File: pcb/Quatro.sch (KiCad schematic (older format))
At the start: 96 parts, among them J1 BATTERY, J2 BATTERY, J3 Conn_01x02, J4 UART1 SH, J5 st-link SH, J6 2.54mm 02x03, J7 2.54mm 02x03, Q1 IRLML6402, Q2 IRFML8244, Q3 BSS138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

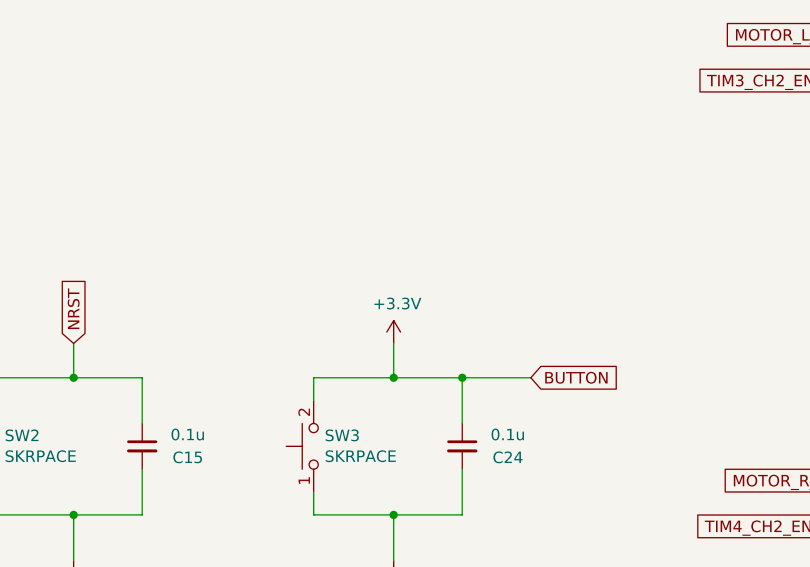
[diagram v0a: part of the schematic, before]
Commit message: プッシュスイッチに抵抗を追加
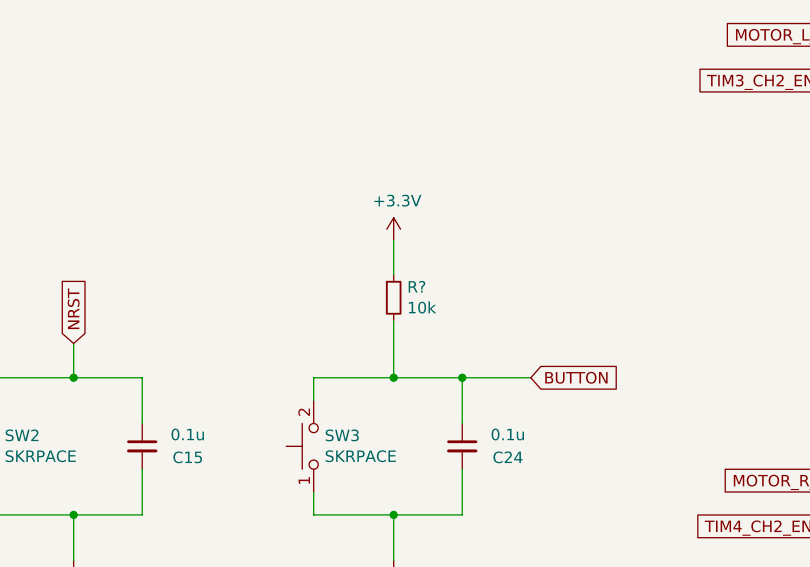
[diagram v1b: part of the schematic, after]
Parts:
- added R?: 10k, Resistor_SMD:R_0603_1608Metric_Pad0.98x0.95mm_HandSolder, symbol Device:R_Small
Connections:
- net +3V3: now also R?.1; no longer C24.1, SW3.2, U7.28 (PB2)
- new net BUTTON: C24.1, R?.2, SW3.2, U7.28 (PB2)
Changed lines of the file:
@@
 Wire Wire Line
 	7800 7500 7800 7600
-Wire Wire Line
-	8150 7500 8150 7350
 $Comp
 L power:GND #PWR0102
@@
 L power:+3.3V #PWR0103
 U 1 1 61A2DF5B
-P 8150 7350
-F 0 "#PWR0103" H 8150 7200 50  0001 C CNN
-F 1 "+3.3V" H 8165 7523 50  0000 C CNN
-F 2 "" H 8150 7350 50  0001 C CNN
-F 3 "" H 8150 7350 50  0001 C CNN
-	1    8150 7350
+P 8150 6900
+F 0 "#PWR0103" H 8150 6750 50  0001 C CNN
+F 1 "+3.3V" H 8165 7073 50  0000 C CNN
+F 2 "" H 8150 6900 50  0001 C CNN
+F 3 "" H 8150 6900 50  0001 C CNN
+	1    8150 6900
 	1    0    0    -1
 $EndComp
@@
 Wire Wire Line
 	13250 4650 13250 4400
+$Comp
+L Device:R_Small R?
+U 1 1 61A509AA
+P 8150 7150
+F 0 "R?" H 8209 7196 50  0000 L CNN
+F 1 "10k" H 8209 7105 50  0000 L CNN
+F 2 "Resistor_SMD:R_0603_1608Metric_Pad0.98x0.95mm_HandSolder" H 8150 7150 50  0001 C CNN
+F 3 "~" H 8150 7150 50  0001 C CNN
+	1    8150 7150
+	1    0    0    -1
+$EndComp
+Wire Wire Line
+	8150 7250 8150 7500
+Wire Wire Line
+	8150 7050 8150 6900
 $EndSCHEMATC

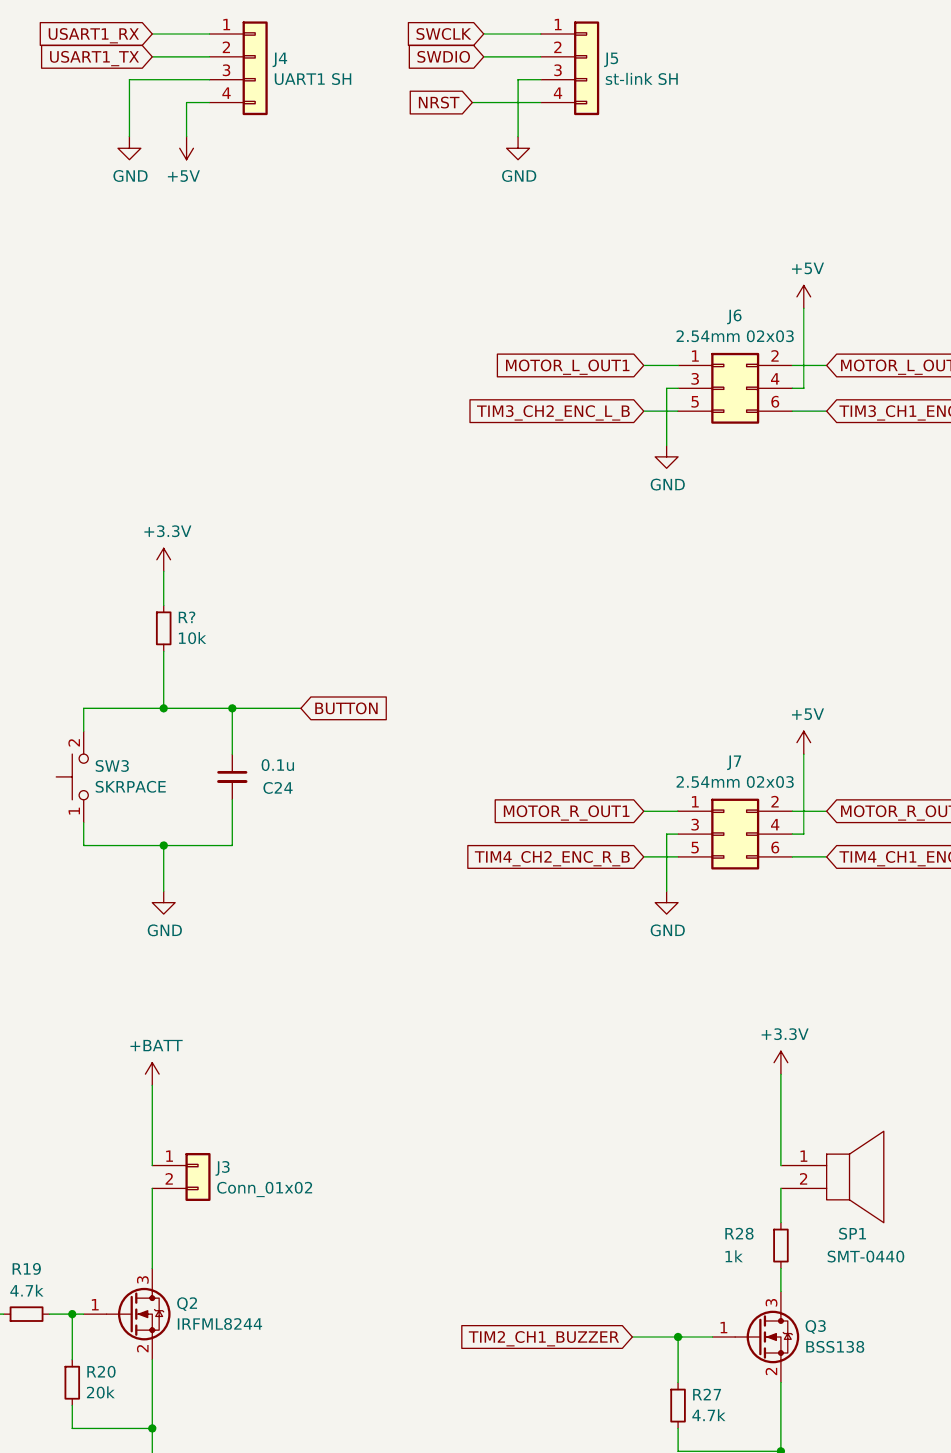
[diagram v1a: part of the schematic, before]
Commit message: 回路を修正してフットプリントを配置した
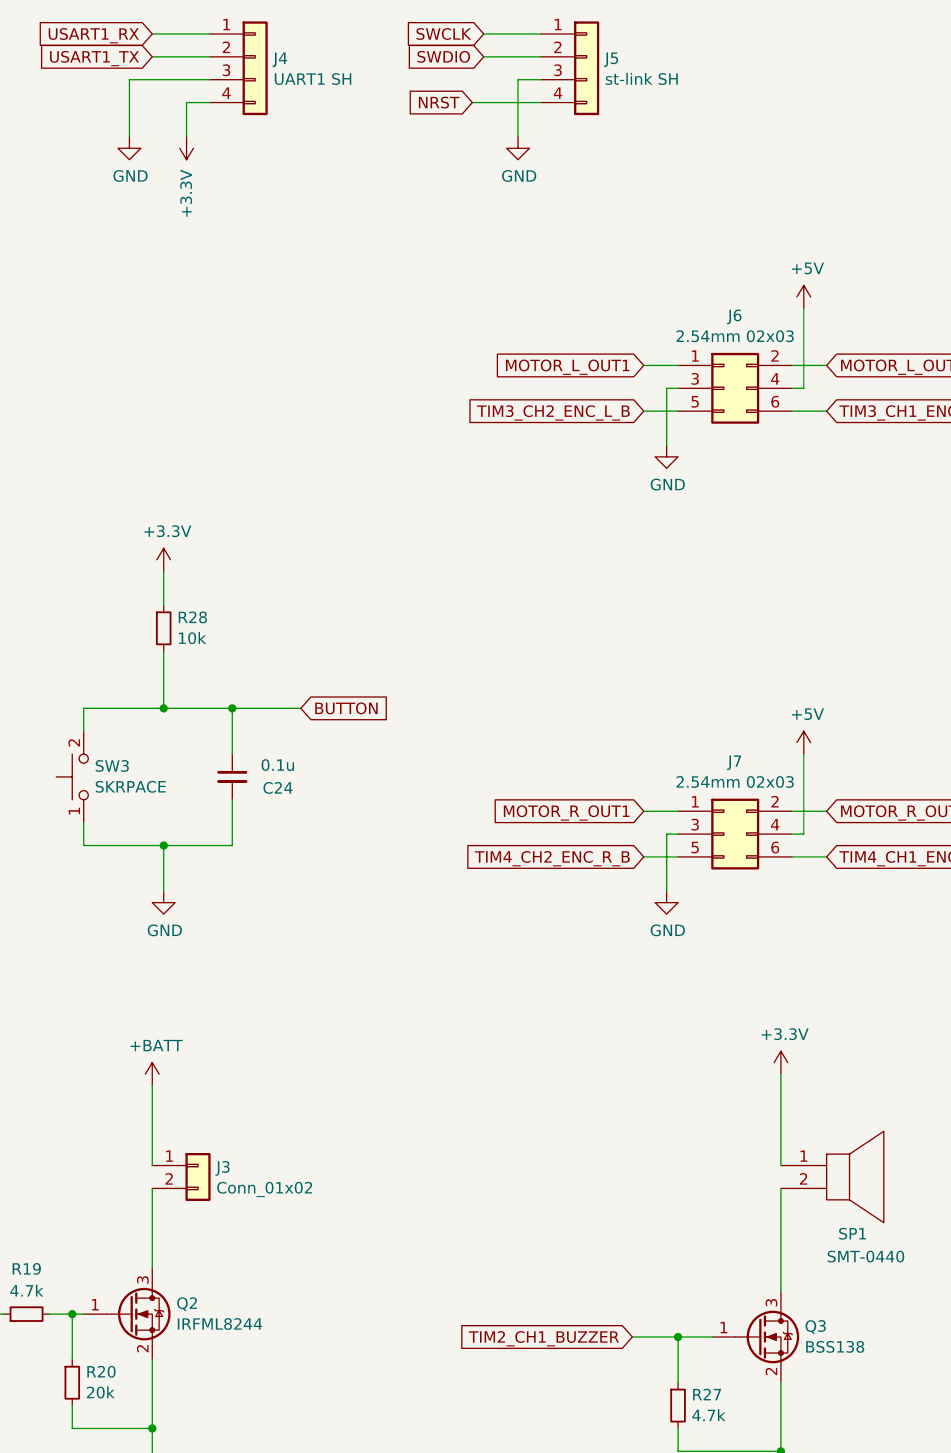
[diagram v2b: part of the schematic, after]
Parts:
- removed R28: 1k, Resistor_SMD:R_0805_2012Metric_Pad1.20x1.40mm_HandSolder, symbol Device:R_Small
- J4: footprint Connector_JST:JST_SH_BM04B-SRSS-TB_1x04-1MP_P1.00mm_Vertical -> Connector_PinHeader_2.54mm:PinHeader_1x04_P2.54mm_Vertical
- gave numbers to parts that had none: 1
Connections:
- net +3V3: now also J4.4 (Pin_4)
- net +5V: no longer J4.4 (Pin_4)
- net at SP1.2: now also Q3.3 (D)
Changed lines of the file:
@@
 $EndComp
 $Comp
-L My_Device:SMT-0440 SP1
-U 1 1 60C7C05A
-P 11050 9450
-F 0 "SP1" H 11100 9100 50  0000 L CNN
-F 1 "SMT-0440" H 11050 9000 50  0000 L CNN
-F 2 "My_Device:SMT-0440-T-R" H 11200 9650 50  0001 C CNN
-F 3 "https://www.puiaudio.com/media/SpecSheet/SMT-0440-T-R.pdf" H 11200 9650 50  0001 C CNN
-	1    11050 9450
-	1    0    0    -1
-$EndComp
-$Comp
 L Device:R_Small R13
 U 1 1 60CC1B37
@@
 F 0 "J4" H 8630 4642 50  0000 L CNN
 F 1 "UART1 SH" H 8630 4551 50  0000 L CNN
-F 2 "Connector_JST:JST_SH_BM04B-SRSS-TB_1x04-1MP_P1.00mm_Vertical" H 8550 4650 50  0001 C CNN
+F 2 "Connector_PinHeader_2.54mm:PinHeader_1x04_P2.54mm_Vertical" H 8550 4650 50  0001 C CNN
 F 3 "~" H 8550 4650 50  0001 C CNN
 	1    8550 4650
@@
 	1    0    0    -1
 $EndComp
-$Comp
-L power:+5V #PWR059
-U 1 1 614C941A
-P 8250 5000
-F 0 "#PWR059" H 8250 4850 50  0001 C CNN
-F 1 "+5V" H 8265 5173 50  0000 C CNN
-F 2 "" H 8250 5000 50  0001 C CNN
-F 3 "" H 8250 5000 50  0001 C CNN
-	1    8250 5000
-	-1   0    0    1
-$EndComp
 Text GLabel 4300 7950 0    50   Input ~ 0
 TIM10_CH1_IR_LED_INNER
@@
 Wire Wire Line
 	12550 1450 12550 1800
-$Comp
-L Connector_Generic:Conn_01x04 J5
-U 1 1 61A31DB2
-P 10000 4650
-F 0 "J5" H 10080 4642 50  0000 L CNN
-F 1 "st-link SH" H 10080 4551 50  0000 L CNN
-F 2 "Connector_JST:JST_SH_BM04B-SRSS-TB_1x04-1MP_P1.00mm_Vertical" H 10000 4650 50  0001 C CNN
-F 3 "~" H 10000 4650 50  0001 C CNN
-	1    10000 4650
-	1    0    0    -1
-$EndComp
 Text GLabel 9550 4550 0    50   Input ~ 0
 SWCLK
@@
 $EndComp
 $Comp
-L Device:R_Small R28
-U 1 1 61799180
-P 10850 9850
-F 0 "R28" H 10600 9900 50  0000 L CNN
-F 1 "1k" H 10600 9800 50  0000 L CNN
-F 2 "Resistor_SMD:R_0805_2012Metric_Pad1.20x1.40mm_HandSolder" H 10850 9850 50  0001 C CNN
-F 3 "~" H 10850 9850 50  0001 C CNN
-	1    10850 9850
-	1    0    0    -1
-$EndComp
-Wire Wire Line
-	10850 9600 10850 9750
-Wire Wire Line
-	10850 9950 10850 10050
-$Comp
 L Connector_Generic:Conn_01x02 J2
 U 1 1 61788A01
@@
 	13250 4650 13250 4400
 $Comp
-L Device:R_Small R?
+L Device:R_Small R28
 U 1 1 61A509AA
 P 8150 7150
-F 0 "R?" H 8209 7196 50  0000 L CNN
+F 0 "R28" H 8209 7196 50  0000 L CNN
 F 1 "10k" H 8209 7105 50  0000 L CNN
 F 2 "Resistor_SMD:R_0603_1608Metric_Pad0.98x0.95mm_HandSolder" H 8150 7150 50  0001 C CNN
@@
 Wire Wire Line
 	8150 7050 8150 6900
+$Comp
+L My_Device:SMT-0440 SP1
+U 1 1 60C7C05A
+P 11050 9450
+F 0 "SP1" H 11100 9100 50  0000 L CNN
+F 1 "SMT-0440" H 11050 9000 50  0000 L CNN
+F 2 "My_Device:SMT-0440-T-R" H 11200 9650 50  0001 C CNN
+F 3 "https://www.puiaudio.com/media/SpecSheet/SMT-0440-T-R.pdf" H 11200 9650 50  0001 C CNN
+	1    11050 9450
+	1    0    0    -1
+$EndComp
+$Comp
+L Connector_Generic:Conn_01x04 J5
+U 1 1 61A31DB2
+P 10000 4650
+F 0 "J5" H 10080 4642 50  0000 L CNN
+F 1 "st-link SH" H 10080 4551 50  0000 L CNN
+F 2 "Connector_JST:JST_SH_BM04B-SRSS-TB_1x04-1MP_P1.00mm_Vertical" H 10000 4650 50  0001 C CNN
+F 3 "~" H 10000 4650 50  0001 C CNN
+	1    10000 4650
+	1    0    0    -1
+$EndComp
+Wire Wire Line
+	10850 9600 10850 10050
+$Comp
+L power:+3.3V #PWR0104
+U 1 1 63400049
+P 8250 5000
+F 0 "#PWR0104" H 8250 4850 50  0001 C CNN
+F 1 "+3.3V" V 8250 5250 50  0000 C CNN
+F 2 "" H 8250 5000 50  0001 C CNN
+F 3 "" H 8250 5000 50  0001 C CNN
+	1    8250 5000
+	-1   0    0    1
+$EndComp
 $EndSCHEMATC
